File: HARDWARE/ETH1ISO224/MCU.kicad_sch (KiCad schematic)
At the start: 38 parts, among them J401 20021111-00010T4LF, U401 LT6350xMS8, U402 REF1933AIDDCT, U403 STM32H743VITx, U404 24LC08B-E/MS, Y401 NX5032GA-16

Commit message: Hardware design
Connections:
- net +1V25 renamed VCOM
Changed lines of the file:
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@@
+	)
+	(symbol
+		(lib_id "power:VCOM")
+		(at 41.91 93.98 180)
+		(unit 1)
+		(exclude_from_sim no)
+		(in_bom yes)
+		(on_board yes)
+		(dnp no)
+		(fields_autoplaced yes)
+		(property "Reference" "#PWR0407"
+			(at 41.91 90.17 0)
+			(effects
+				(font
+					(size 1.27 1.27)
+				)
+				(hide yes)
+			)
+		)
+		(property "Value" "VCOM"
+			(at 41.91 99.06 0)
+			(effects
+				(font
+					(size 1.27 1.27)
+				)
+			)
+		)
+		(property "Footprint" ""
+			(at 41.91 93.98 0)
+			(effects
+				(font
+					(size 1.27 1.27)
+				)
+				(hide yes)
+			)
+		)
+		(property "Datasheet" ""
+			(at 41.91 93.98 0)
+			(effects
+				(font
+					(size 1.27 1.27)
+				)
+				(hide yes)
+			)
+		)
+		(property "Description" "Power symbol creates a global label with name \"VCOM\""
+			(at 41.91 93.98 0)
+			(effects
+				(font
+					(size 1.27 1.27)
+				)
+				(hide yes)
+			)
+		)
+		(pin "1"
+		)
+		(instances
+			(project "ETH1ISO224"
+				(path "/093d5244-f12f-48bc-bb5b-bcbdc8fa59fa/0064cd61-5529-40f7-bb6b-05e681e46275"
+					(reference "#PWR0407")
+					(unit 1)
+				)
+			)
+		)
 	)
 	(symbol
@@
 					(unit 1)
 				)
-			)
-		)
-	)
-	(symbol
-		(lib_id "ETH1ISO224:+1V25")
-		(at 41.91 93.98 180)
-		(unit 1)
-		(exclude_from_sim no)
-		(in_bom yes)
-		(on_board yes)
-		(dnp no)
-		(property "Reference" "#PWR0407"
-			(at 41.91 90.17 0)
-			(effects
-				(font
-					(size 1.27 1.27)
-				)
-				(hide yes)
-			)
-		)
-		(property "Value" "+1V25"
-			(at 41.91 98.298 0)
-			(effects
-				(font
-					(size 1.27 1.27)
-				)
-			)
-		)
-		(property "Footprint" ""
-			(at 41.91 93.98 0)
-			(effects
-				(font
-					(size 1.27 1.27)
-				)
-				(hide yes)
-			)
-		)
-		(property "Datasheet" ""
-			(at 41.91 93.98 0)
-			(effects
-				(font
-					(size 1.27 1.27)
-				)
-				(hide yes)
-			)
-		)
-		(property "Description" "Power symbol creates a global label with name \"+1V25\""
-			(at 41.91 93.98 0)
-			(effects
-				(font
-					(size 1.27 1.27)
-				)
-				(hide yes)
-			)
-		)
-		(pin "1"
-		)
-		(instances
-			(project "ETH1ISO224"
-				(path "/093d5244-f12f-48bc-bb5b-bcbdc8fa59fa/0064cd61-5529-40f7-bb6b-05e681e46275"
-					(reference "#PWR0407")
-					(unit 1)
-				)

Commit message: Hardware design
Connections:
- net LED_RED: now also U403.66 (PC9); no longer U403.64 (PC7)
- net MCU_G1: now also U403.29 (PA5); no longer U403.36 (PB2)
- net MCU_G10: now also U403.28 (PA4); no longer U403.29 (PA5)
- net MCU_G100: now also U403.25 (PA3); no longer U403.28 (PA4)
- net MCU_ZOFFS: now also U403.30 (PA6); no longer U403.35 (PB1)
- net +5V renamed +5VA
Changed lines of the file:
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@@
 	)
 	(no_connect
-		(at 187.96 44.45)
-	)
-	(no_connect
 		(at 144.78 90.17)
 	)
@@
 	)
 	(no_connect
+		(at 187.96 74.93)
+	)
+	(no_connect
 		(at 144.78 118.11)
 	)
@@
 	)
 	(no_connect
+		(at 187.96 77.47)
+	)
+	(no_connect
 		(at 187.96 49.53)
 	)
@@
 	)
 	(no_connect
-		(at 187.96 138.43)
-	)
-	(no_connect
 		(at 144.78 130.81)
 	)
@@
 	)
 	(no_connect
-		(at 187.96 36.83)
-	)
-	(no_connect
 		(at 187.96 52.07)
 	)
@@
 	)
 	(no_connect
+		(at 187.96 133.35)
+	)
+	(no_connect
 		(at 233.68 152.4)
 	)
@@
 	(wire
 		(pts
-			(xy 189.23 77.47) (xy 187.96 77.47)
+			(xy 189.23 41.91) (xy 187.96 41.91)
 		)
 		(stroke
@@
 	(wire
 		(pts
-			(xy 187.96 133.35) (xy 212.09 133.35)
+			(xy 187.96 135.89) (xy 212.09 135.89)
 		)
 		(stroke
@@
 	(wire
 		(pts
-			(xy 191.77 39.37) (xy 187.96 39.37)
+			(xy 189.23 36.83) (xy 187.96 36.83)
 		)
 		(stroke
@@
 	(wire
 		(pts
-			(xy 191.77 41.91) (xy 187.96 41.91)
+			(xy 189.23 39.37) (xy 187.96 39.37)
 		)
 		(stroke
@@
 	(wire
 		(pts
-			(xy 189.23 74.93) (xy 187.96 74.93)
+			(xy 189.23 44.45) (xy 187.96 44.45)
 		)
 		(stroke
@@
 	(wire
 		(pts
-			(xy 187.96 135.89) (xy 212.09 135.89)
+			(xy 187.96 138.43) (xy 212.09 138.43)
 		)
 		(stroke
@@
 	)
 	(label "LED_RED"
-		(at 212.09 133.35 180)
+		(at 212.09 138.43 180)
 		(fields_autoplaced yes)
 		(effects
@@
 	(hierarchical_label "MCU_G1"
 		(shape output)
-		(at 189.23 77.47 0)
+		(at 189.23 41.91 0)
 		(fields_autoplaced yes)
 		(effects
@@
 	(hierarchical_label "MCU_G10"
 		(shape output)
-		(at 191.77 41.91 0)
+		(at 189.23 39.37 0)
 		(fields_autoplaced yes)
 		(effects
@@
 	(hierarchical_label "MCU_ZOFFS"
 		(shape output)
-		(at 189.23 74.93 0)
+		(at 189.23 44.45 0)
 		(fields_autoplaced yes)
 		(effects
@@
 	(hierarchical_label "MCU_G100"
 		(shape output)
-		(at 191.77 39.37 0)
+		(at 189.23 36.83 0)
 		(fields_autoplaced yes)
 		(effects
@@
 	)
 	(symbol
-		(lib_id "power:+5V")
+		(lib_id "power:+5VA")
 		(at 50.8 119.38 0)
 		(unit 1)
@@
 		(dnp no)
 		(fields_autoplaced yes)
-		(property "Reference" "#PWR0410"
+		(property "Reference" "#PWR0407"
 			(at 50.8 123.19 0)
 			(effects
@@
 			)
 		)
-		(property "Value" "+5V"
-			(at 50.8 115.57 0)
+		(property "Value" "+5VA"
+			(at 50.8 114.3 0)
 			(effects
 				(font
@@
 			)
 		)
-		(property "Description" "Power symbol creates a global label with name \"+5V\""
+		(property "Description" "Power symbol creates a global label with name \"+5VA\""
 			(at 50.8 119.38 0)
 			(effects
@@
 			(project "ETH1ISO224"
 				(path "/093d5244-f12f-48bc-bb5b-bcbdc8fa59fa/0064cd61-5529-40f7-bb6b-05e681e46275"
-					(reference "#PWR0410")
-					(unit 1)
-				)
-			)
-			(project "ETH1HMSR-SMS"
-				(path "/c9f88626-4b87-4d35-a77a-42f8d5451fae/b5799081-919e-4d88-9f68-c3d7000bcf73"
-					(reference "#PWR0410")
+					(reference "#PWR0407")
 					(unit 1)
 				)

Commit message: Hardware design
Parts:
- added C409: 0.1u, Capacitor_SMD:C_0603_1608Metric_Pad1.08x0.95mm_HandSolder, symbol Device:C
- added C411: 1u, Capacitor_SMD:C_0603_1608Metric_Pad1.08x0.95mm_HandSolder, symbol Device:C
- renumbered C409 to C410, C410 to C412, C411 to C413, C412 to C414, C413 to C415, C414 to C416, C415 to C417, C416 to C418, C417 to C419, C418 to C420, C419 to C421, C420 to C422
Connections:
- net GND: now also C409.2, C411.2
- net VCOM: now also U402.1 (Vbias), C409.1, C411.1
- no-connect marks 63 -> 62

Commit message: Hardware design done
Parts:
- U401: value LT6350xMS8 -> LT6350IMS8
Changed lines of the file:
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@@
 			)
 		)
-		(property "Value" "LT6350xMS8"
+		(property "Value" "LT6350IMS8"
 			(at 55.626 74.422 0)
 			(effects

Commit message: Footprint change, not critical
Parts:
- U402: footprint Package_TO_SOT_SMD:SOT-23-5_HandSoldering -> Package_TO_SOT_SMD:SOT-23-5
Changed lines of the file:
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@@
 			)
 		)
-		(property "Footprint" "Package_TO_SOT_SMD:SOT-23-5_HandSoldering"
+		(property "Footprint" "Package_TO_SOT_SMD:SOT-23-5"
 			(at 50.8 130.81 0)
 			(effects

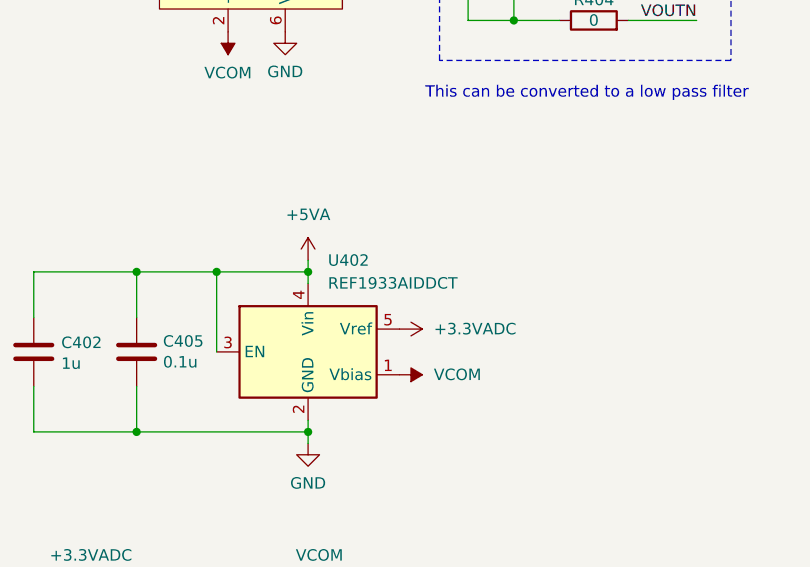
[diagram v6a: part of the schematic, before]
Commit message: Changed REF19 to REF20
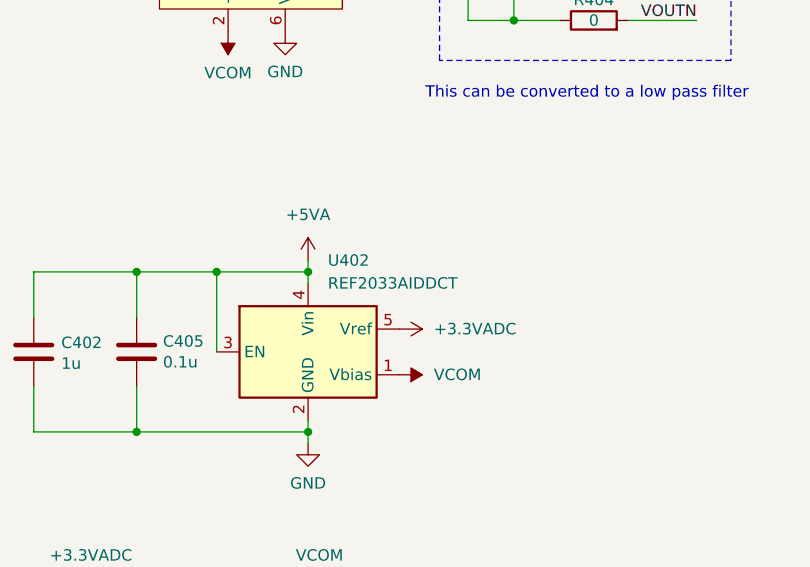
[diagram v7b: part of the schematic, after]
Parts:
- U402: value REF1933AIDDCT -> REF2033AIDDCT
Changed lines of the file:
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@@
 			)
 		)
-		(property "Value" "REF1933AIDDCT"
+		(property "Value" "REF2033AIDDCT"
 			(at 52.9941 121.92 0)
 			(effects
